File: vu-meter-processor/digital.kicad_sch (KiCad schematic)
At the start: 9 parts, among them U3 CH32X035F7P6

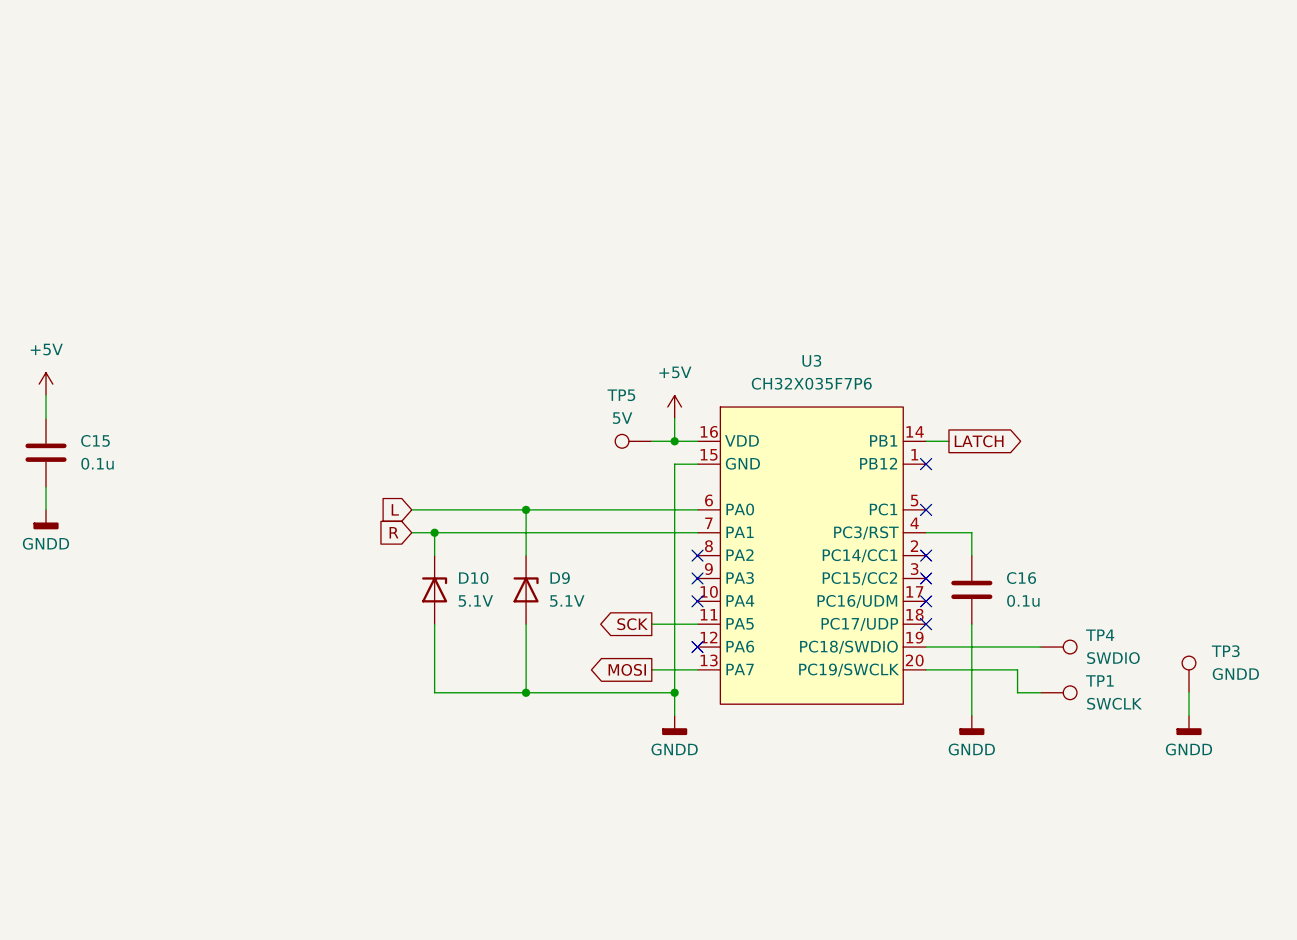
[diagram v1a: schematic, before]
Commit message: remove analog peak detector fully and split one chip into two for better inter-channel performance
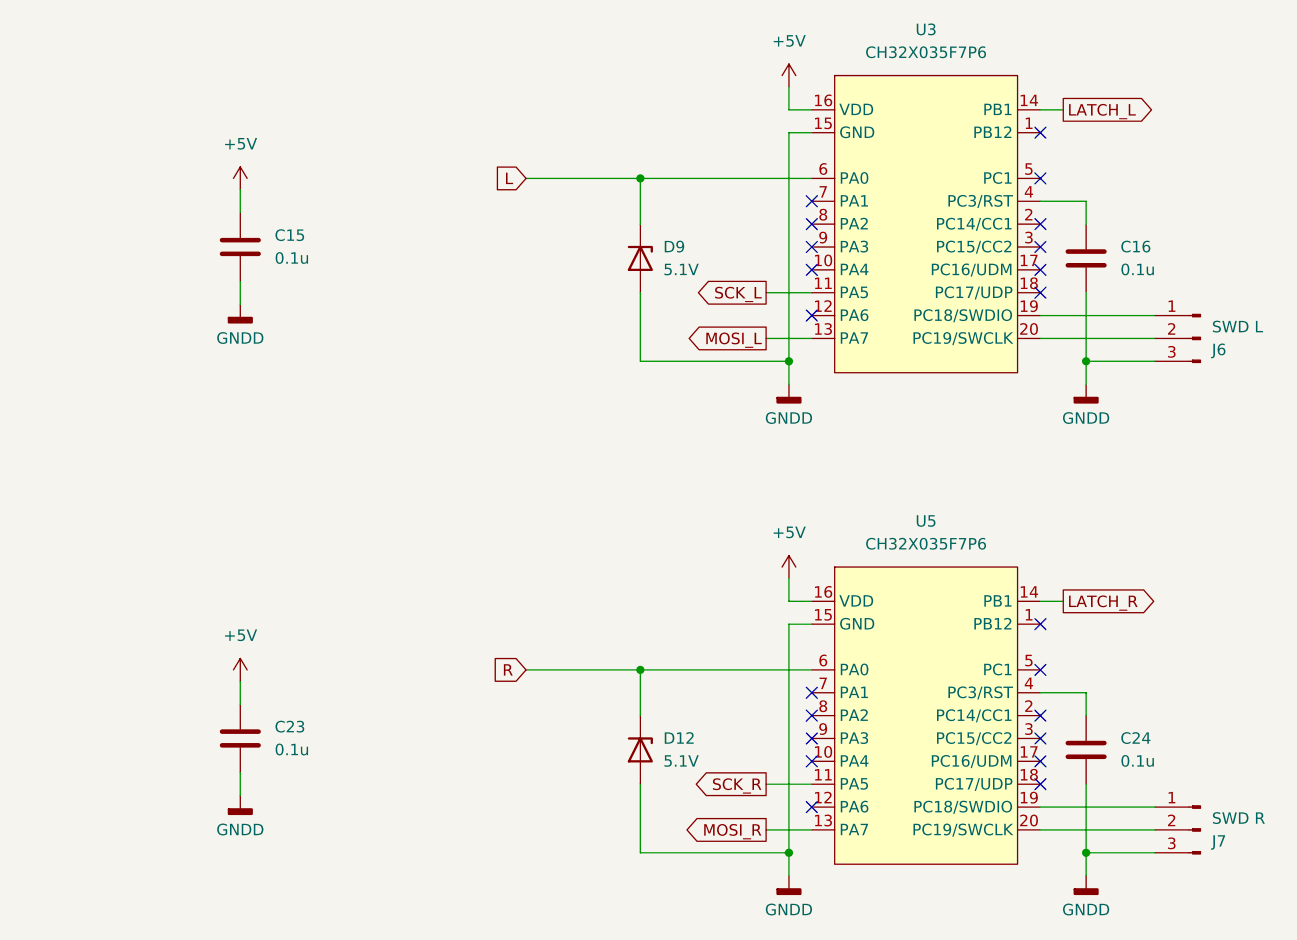
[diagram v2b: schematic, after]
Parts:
- removed D10: 5.1V, Diode_SMD:D_MiniMELF, symbol Device:D_Zener
- removed TP1: SWCLK, TestPoint:TestPoint_Pad_D2.0mm, symbol Connector:TestPoint
- removed TP3: GNDD, TestPoint:TestPoint_Pad_D2.0mm, symbol Connector:TestPoint
- removed TP4: SWDIO, TestPoint:TestPoint_Pad_D2.0mm, symbol Connector:TestPoint
- removed TP5: 5V, TestPoint:TestPoint_Pad_D2.0mm, symbol Connector:TestPoint
- added C23, C24: 0.1u, Capacitor_SMD:C_0805_2012Metric, symbol Device:C
- added D12: 5.1V, Diode_SMD:D_MiniMELF, symbol Device:D_Zener
- added J6: SWD L, Connector_PinHeader_2.54mm:PinHeader_1x03_P2.54mm_Vertical, symbol Connector:Conn_01x03_Pin
- added J7: SWD R, Connector_PinHeader_2.54mm:PinHeader_1x03_P2.54mm_Vertical, symbol Connector:Conn_01x03_Pin
- added U5: CH32X035F7P6, Package_SO:TSSOP-20_4.4x6.5mm_P0.65mm, symbol Custom_Symbols:CH32X035F7P6
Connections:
- net +5V: now also C23.1, U5.16 (VDD)
- net GNDD: now also C23.2, C24.2, D12.2 (A), J6.3 (Pin_3), J7.3 (Pin_3), U5.15 (GND)
- net R: now also D12.1 (K), U5.6 (PA0); no longer U3.7 (PA1)
- net at U3.19 (PC18/SWDIO): now also J6.1 (Pin_1)
- net at U3.20 (PC19/SWCLK): now also J6.2 (Pin_2)
- net LATCH renamed LATCH_L
- net MOSI renamed MOSI_L
- net SCK renamed SCK_L
- new net: J7.1 (Pin_1), U5.19 (PC18/SWDIO)
- new net: J7.2 (Pin_2), U5.20 (PC19/SWCLK)
- new net: C24.1, U5.4 (PC3/RST)
- new net LATCH_R: U5.14 (PB1)
- new net MOSI_R: U5.13 (PA7)
- new net SCK_R: U5.11 (PA5)
- no-connect marks 10 -> 22
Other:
- moved on the sheet: C15, C16, D9, U3
